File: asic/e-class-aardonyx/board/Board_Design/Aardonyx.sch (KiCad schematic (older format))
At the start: 0 parts

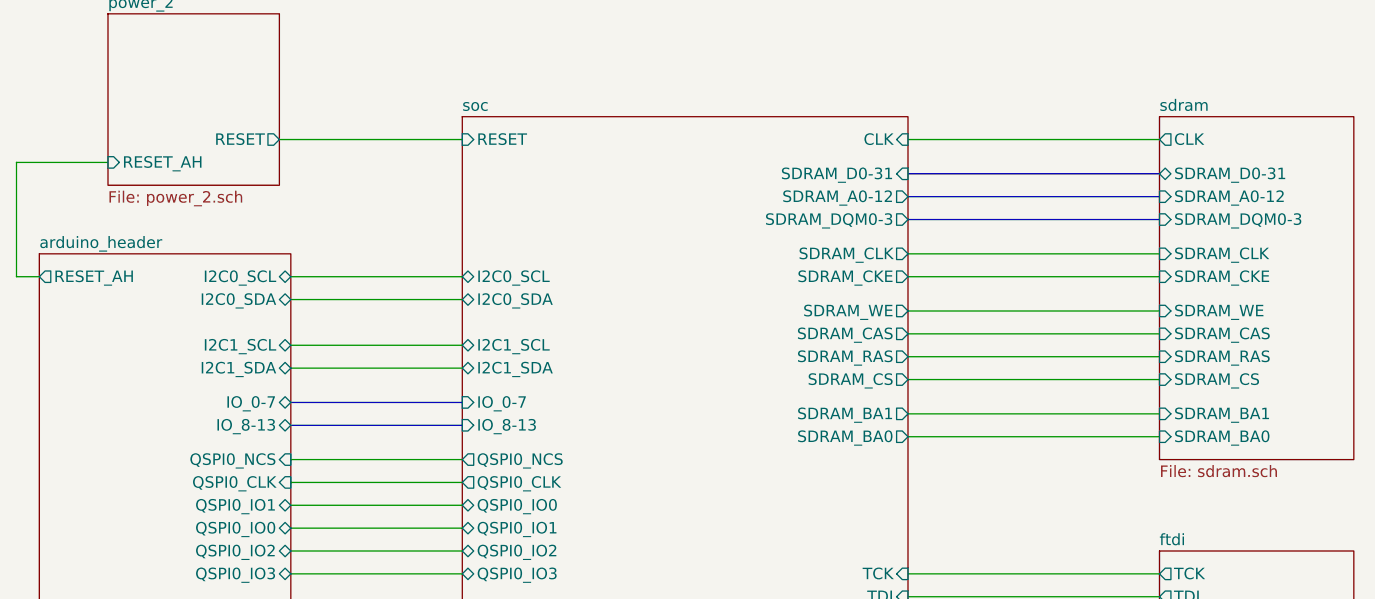
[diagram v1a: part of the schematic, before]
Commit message: updated commented pending schematic
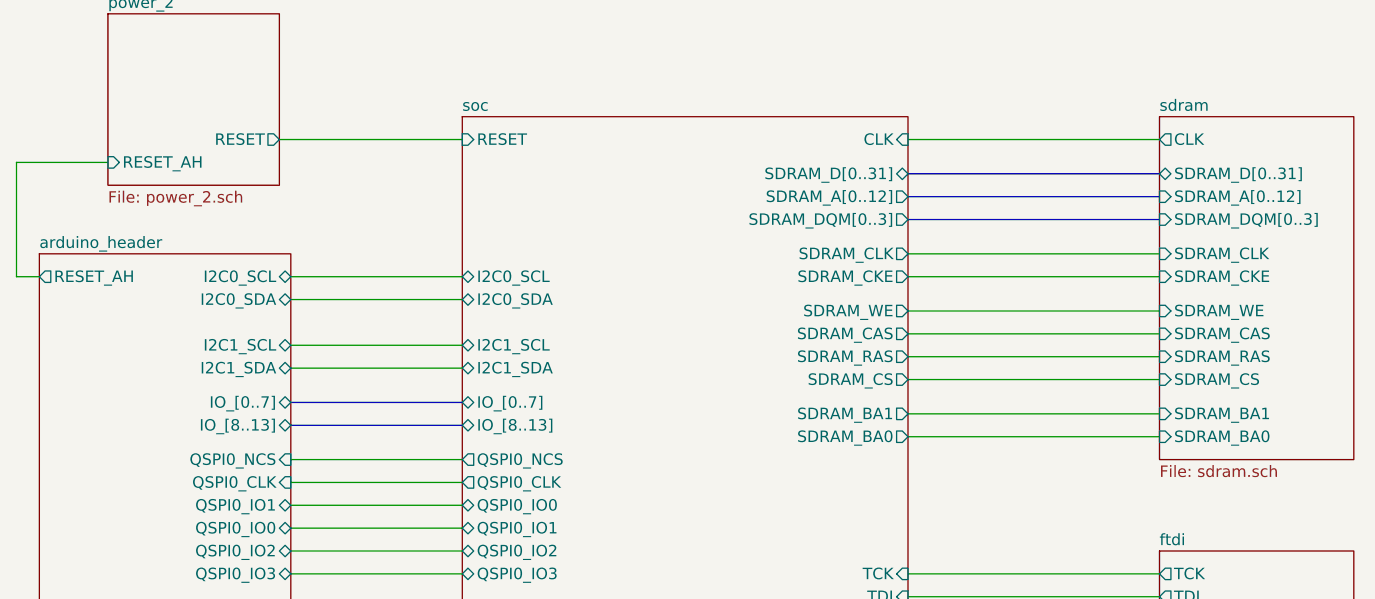
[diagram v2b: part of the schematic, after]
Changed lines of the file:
@@
 F0 "sdram" 50
 F1 "sdram.sch" 50
-F2 "SDRAM_A0-12" I L 8150 2550 50
-F3 "SDRAM_D0-31" B L 8150 2450 50
-F4 "SDRAM_DQM0-3" I L 8150 2650 50
-F5 "CLK" O L 8150 2300 50
-F6 "SDRAM_CKE" I L 8150 2900 50
-F7 "SDRAM_CLK" I L 8150 2800 50
-F8 "SDRAM_WE" I L 8150 3050 50
-F9 "SDRAM_CAS" I L 8150 3150 50
-F10 "SDRAM_RAS" I L 8150 3250 50
-F11 "SDRAM_CS" I L 8150 3350 50
-F12 "SDRAM_BA1" I L 8150 3500 50
-F13 "SDRAM_BA0" I L 8150 3600 50
+F2 "SDRAM_D[0..31]" B L 8150 2450 50
+F3 "CLK" O L 8150 2300 50
+F4 "SDRAM_CKE" I L 8150 2900 50
+F5 "SDRAM_CLK" I L 8150 2800 50
+F6 "SDRAM_WE" I L 8150 3050 50
+F7 "SDRAM_CAS" I L 8150 3150 50
+F8 "SDRAM_RAS" I L 8150 3250 50
+F9 "SDRAM_CS" I L 8150 3350 50
+F10 "SDRAM_BA1" I L 8150 3500 50
+F11 "SDRAM_BA0" I L 8150 3600 50
+F12 "SDRAM_A[0..12]" I L 8150 2550 50
+F13 "SDRAM_DQM[0..3]" I L 8150 2650 50
 $EndSheet
 $Sheet
@@
 Wire Wire Line
 	7050 2300 8150 2300
-Wire Bus Line
-	7050 2450 8150 2450
 Wire Bus Line
 	7050 2550 8150 2550
@@
 F6 "QSPI0_CLK" I R 4350 3800 50
 F7 "QSPI0_NCS" I R 4350 3700 50
-F8 "IO_0-7" B R 4350 3450 50
-F9 "IO_8-13" B R 4350 3550 50
-F10 "I2C1_SCL" B R 4350 3200 50
-F11 "I2C1_SDA" B R 4350 3300 50
-F12 "SPI0_MISO" O R 4350 4600 50
-F13 "SPI0_MOSI" I R 4350 4700 50
-F14 "SPI0_CLK" I R 4350 4400 50
-F15 "SPI0_nCS" I R 4350 4500 50
-F16 "I2C0_SCL" B R 4350 2900 50
-F17 "I2C0_SDA" B R 4350 3000 50
-F18 "SPI1_nCS" I R 4350 5000 50
-F19 "SPI1_CLK" I R 4350 5100 50
-F20 "SPI1_MISO" O R 4350 5200 50
-F21 "SPI1_MOSI" I R 4350 5300 50
-F22 "RESET_AH" O L 3250 2900 50
-F23 "IO_14" B R 4350 5500 50
-F24 "IO_15" B R 4350 5600 50
+F8 "I2C1_SCL" B R 4350 3200 50
+F9 "I2C1_SDA" B R 4350 3300 50
+F10 "SPI0_MISO" O R 4350 4600 50
+F11 "SPI0_MOSI" I R 4350 4700 50
+F12 "SPI0_CLK" I R 4350 4400 50
+F13 "SPI0_nCS" I R 4350 4500 50
+F14 "I2C0_SCL" B R 4350 2900 50
+F15 "I2C0_SDA" B R 4350 3000 50
+F16 "SPI1_nCS" I R 4350 5000 50
+F17 "SPI1_CLK" I R 4350 5100 50
+F18 "SPI1_MISO" O R 4350 5200 50
+F19 "SPI1_MOSI" I R 4350 5300 50
+F20 "RESET_AH" O L 3250 2900 50
+F21 "IO_14" B R 4350 5500 50
+F22 "IO_15" B R 4350 5600 50
+F23 "IO_[8..13]" B R 4350 3550 50
+F24 "IO_[0..7]" B R 4350 3450 50
 $EndSheet
 Wire Wire Line
@@
 F27 "UART0_TX" O R 7050 4750 50
 F28 "UART0_RX" I R 7050 4850 50
-F29 "SDRAM_D0-31" I R 7050 2450 50
+F29 "SDRAM_D[0..31]" B R 7050 2450 50
 F30 "SDRAM_CKE" O R 7050 2900 50
 F31 "SDRAM_CLK" O R 7050 2800 50
@@
 F36 "SDRAM_BA1" O R 7050 3500 50
 F37 "SDRAM_BA0" O R 7050 3600 50
-F38 "SDRAM_DQM0-3" O R 7050 2650 50
-F39 "SDRAM_A0-12" O R 7050 2550 50
-F40 "IO_0-7" I L 5100 3450 50
-F41 "IO_8-13" I L 5100 3550 50
-F42 "IO_14" B L 5100 5500 50
-F43 "IO_15" B L 5100 5600 50
+F38 "IO_14" B L 5100 5500 50
+F39 "IO_15" B L 5100 5600 50
+F40 "SDRAM_A[0..12]" O R 7050 2550 50
+F41 "SDRAM_DQM[0..3]" O R 7050 2650 50
+F42 "IO_[0..7]" B L 5100 3450 50
+F43 "IO_[8..13]" B L 5100 3550 50
 $EndSheet
 Wire Wire Line
@@
 Wire Wire Line
 	5100 5600 4350 5600
+Wire Bus Line
+	7050 2450 8150 2450
 $EndSCHEMATC

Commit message: Updated schematic
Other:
- note added: "AARDONYX SKT32E - DEVELOPMENT BOARD"
- note added: "WITH ARDUINO COMPATIBLE HEADERS"
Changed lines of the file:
@@
 EESchema Schematic File Version 4
-EELAYER 30 0
+LIBS:Aardonyx-cache
+EELAYER 29 0
 EELAYER END
 $Descr A4 11693 8268
 encoding utf-8
 Sheet 1 7
-Title "AARDONYX_DEVELOPMENT_BOARD"
+Title "AARDONYX SKT32E DEVELOPMENT BOARD"
 Date ""
 Rev "R1V0"
@@
 Comment1 ""
 Comment2 ""
-Comment3 ""
-Comment4 ""
+Comment3 "Aardonyx - SKT32E"
+Comment4 "Hierarchial Sheet"
 $EndDescr
 $Sheet
@@
 Wire Bus Line
 	7050 2450 8150 2450
+Text Notes 4600 1050 0    100  ~ 20
+AARDONYX SKT32E - DEVELOPMENT BOARD
+Text Notes 4700 1300 0    100  ~ 20
+WITH ARDUINO COMPATIBLE HEADERS
 $EndSCHEMATC
